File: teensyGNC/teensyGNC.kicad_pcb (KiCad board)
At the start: 4 copper layers, 53 x 139.5 mm, 46 parts, among them J1 ESC_1_PWM, J10 ToF_OF_SH, J11 Hall_1_PH, J12 Hall_2_PH, J13 Hall_3_PH, J14 Hall_4_PH, J2 5V_In_XH, J3 ESC_2_PWM, J4 Servo_1_PWM, J5 Servo_2_PWM, J6 7V4_In, J7 Ebyte, J8 LC29H, J9 Batt_Mon_GH, U1 E28-2G4T20SX, U2 4754, U3 AP2112K-3.3, U4 4494, U5 Teensy4.1

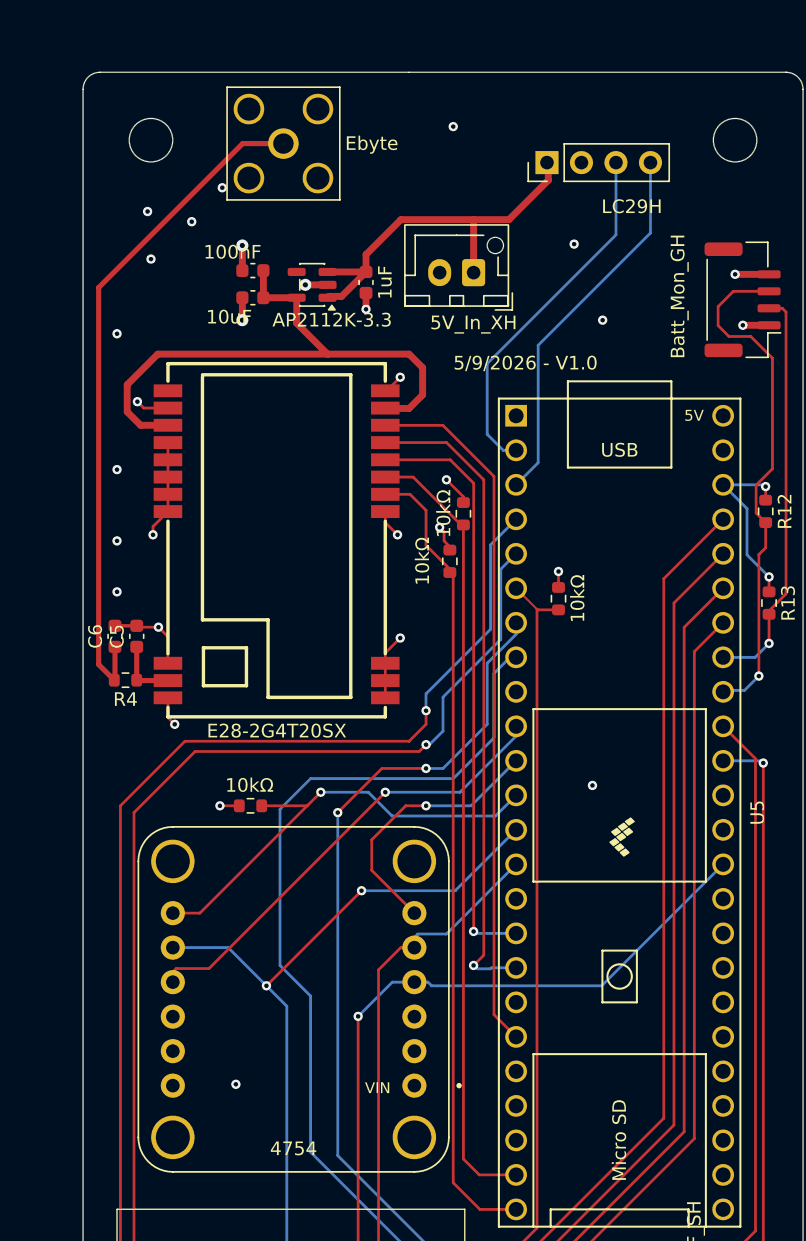
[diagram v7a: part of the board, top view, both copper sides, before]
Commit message: V1.0 Order placed at JLCPCB
- Some components changed to basic versions to lower cost a bit (TOTAL 96 USD!!!?? Do try and lower further for future versions, main cost seems to be extended part fees, maybe look into more hand soldered bits?)
- Some JST connectors bought on taobao and assembled myself
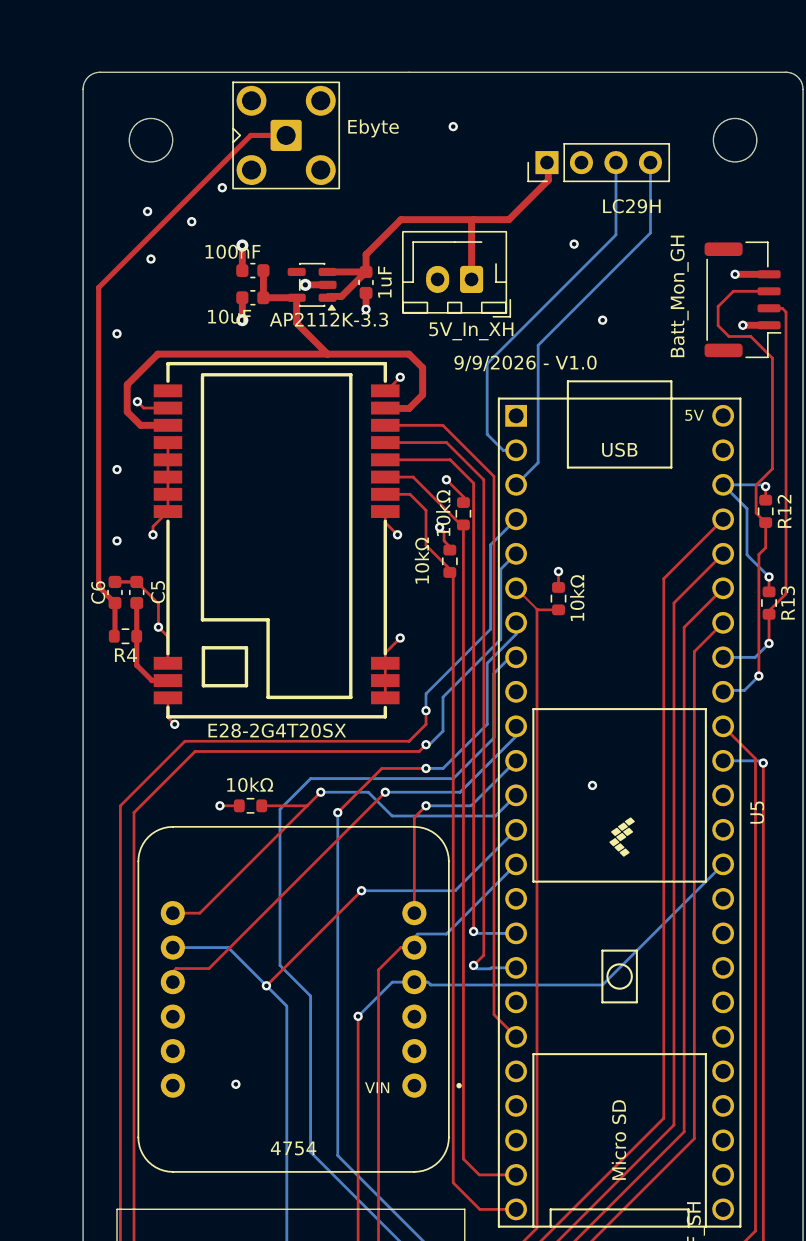
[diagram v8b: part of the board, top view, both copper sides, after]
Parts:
- J7: footprint Connector_Coaxial:SMA_Amphenol_132203-12_Horizontal -> Connector_Coaxial:SMA_BAT_Wireless_BWSMA-KWE-Z001
- moved C5 3.23 mm to (75.2, 75.0)
- moved C6 3.23 mm to (73.6, 75.0)
- moved R4 3.23 mm to (74.4, 78.3)
- moved J2 1.49 mm to (98.6, 52.0)
- moved J7 0.63 mm to (86.2, 41.4)
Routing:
- net Net-(J7-In): track 49.9 -> 44.7 mm
- net /SPI.INT: track 19.7 -> 16.3 mm
- net Net-(U1-ANT): track 4.94 -> 7.57 mm
- net GND: track 67.6 -> 69.9 mm, vias 44 -> 43
- net +5V: track 140.0 -> 140.5 mm
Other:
- board text added: "9/9/2026 - V1.0"
- board text removed: "5/9/2026 - V1.0"
